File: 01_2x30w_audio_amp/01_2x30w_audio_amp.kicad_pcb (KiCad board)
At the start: 4 copper layers, 90 x 90 mm, 90 parts, among them J101 CUI 5.08mm, J102 SSQ-107-03-T-D, J103 SSQ-120-03-T-D, J104 CUI 5.08mm, J105 CUI 5.08mm, J108 CUI 5.08mm, J109 CUI 5.08mm, Q101 AON7534, Q201 AON7534, U101 MCP1416, U201 AP64500, U801 TPA3118D2

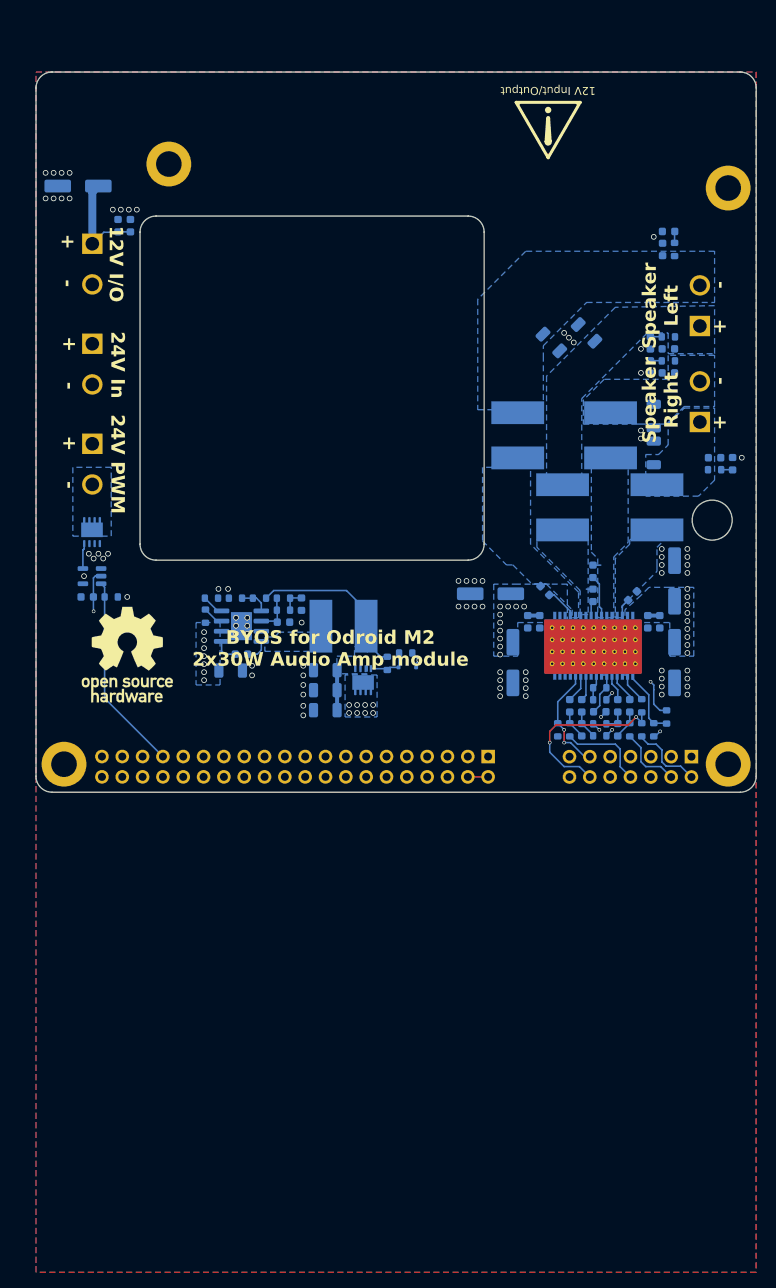
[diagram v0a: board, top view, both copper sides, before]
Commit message: Module no. 1 completely redesigned
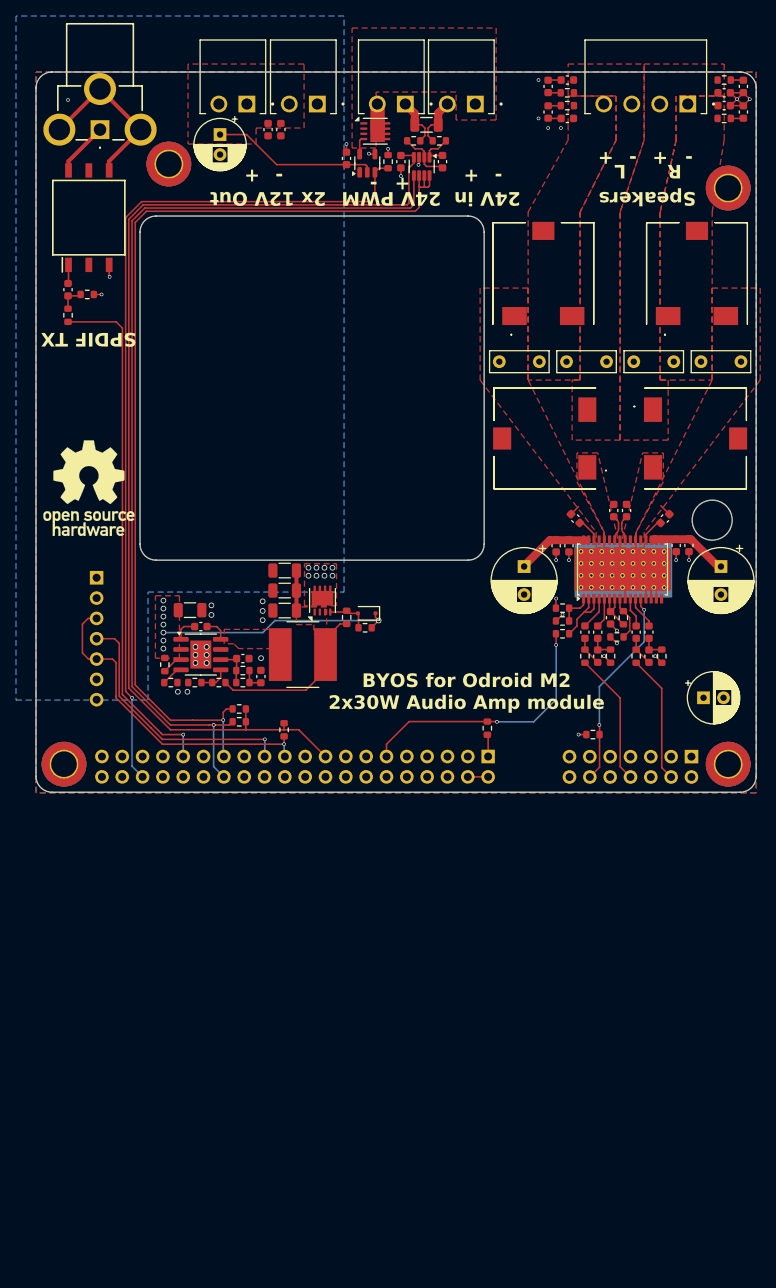
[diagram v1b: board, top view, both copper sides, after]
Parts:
- removed C817, C818, C819: 680n 35V, Capacitor_SMD:C_1206_3216Metric
- removed C820, C821, C826, C827: 865080545012, Capacitor_SMD:C_Elec_6.3x7.7
- removed the J101 at (27.0, 54.0)
- removed the J105 at (103.0, 51.7)
- removed J109: CUI 5.08mm, libs:CUI_TBP01R1-508-02BE
- removed L802, L803, L804: SRN8040TA-100M, Inductor_SMD:L_Bourns_SRN8040TA
- removed SYM102: SYM_Radioactive_Large, Symbol:Symbol_Attention_Triangle_8x7mm_Copper
- added C104: A750EK227M1CAAE016, Capacitor_THT:CP_Radial_D6.3mm_P2.50mm, F.Cu at (43.0, 27.8)
- added C301: 100n, Capacitor_SMD:C_0603_1608Metric, F.Cu at (24.0, 47.2)
- added C401: 100n 25V, Capacitor_SMD:C_0603_1608Metric, F.Cu at (65.6, 31.2)
- added C402: 100n, Capacitor_SMD:C_0603_1608Metric, F.Cu at (70.8, 31.2)
- added C616: B32529C684J, Capacitor_THT:C_Rect_L7.2mm_W2.5mm_P5.00mm_FKS2_FKP2_MKS2_MKP2, F.Cu at (77.9, 56.2)
- added C618: B32529C684J, Capacitor_THT:C_Rect_L7.2mm_W2.5mm_P5.00mm_FKS2_FKP2_MKS2_MKP2, F.Cu at (94.7, 56.2)
- added C619: B32529C684J, Capacitor_THT:C_Rect_L7.2mm_W2.5mm_P5.00mm_FKS2_FKP2_MKS2_MKP2, F.Cu at (108.1, 56.2)
- added C620: A750KS227M1EAAE015, Capacitor_THT:CP_Radial_D8.0mm_P3.50mm, F.Cu at (81.0, 81.8)
- added C621: A750KS227M1EAAE015, Capacitor_THT:CP_Radial_D8.0mm_P3.50mm, F.Cu at (105.6, 81.8)
- added J103: CUI 3.5mm, libs:CUI_TBP03R1-350-02BE, F.Cu at (74.9, 24.0)
- added J104: CUI 3.5mm, libs:CUI_TBP03R1-350-02BE, F.Cu at (66.2, 24.0)
- added J107: CUI 3.5mm, libs:CUI_TBP03R1-350-02BE, F.Cu at (46.4, 24.0)
- added J301: KLPX-0848A, libs:936, F.Cu at (28.0, 27.2)
- added J501: Conn_01x07, Connector_PinSocket_2.54mm:PinSocket_1x07_P2.54mm_Vertical, B.Cu at (27.6, 83.2)
- added L602: RFC0807B-123KE, libs:SER1360182KLD, F.Cu at (83.6, 65.8)
- added L603: RFC0807B-123KE, libs:SER1360182KLD, F.Cu at (102.4, 65.8)
- added L604: RFC0807B-123KE, libs:SER1360182KLD, F.Cu at (102.6, 45.2)
- added R301: 200R, Resistor_SMD:R_0603_1608Metric, F.Cu at (24.0, 50.4)
- added R302: 110R, Resistor_SMD:R_0603_1608Metric, F.Cu at (26.4, 47.8)
- added R401: 10k, Resistor_SMD:R_0603_1608Metric, F.Cu at (45.4, 99.6)
- added R402: 10k, Resistor_SMD:R_0603_1608Metric, F.Cu at (45.4, 101.2)
- added R403: 10R, Resistor_SMD:R_0603_1608Metric, F.Cu at (70.4, 28.6)
- added R404: 30m 1W, Resistor_SMD:R_1206_3216Metric, F.Cu at (68.8, 26.6)
- added R405: 10R, Resistor_SMD:R_0603_1608Metric, F.Cu at (67.2, 28.6)
- added R501: 10k, Resistor_SMD:R_0603_1608Metric, F.Cu at (51.0, 102.2)
- added T301: DA101JC, libs:SOP254P1270X635-6N, F.Cu at (26.6, 38.2)
- added U401: INA219AxDCN, Package_TO_SOT_SMD:SOT-23-8, F.Cu at (68.2, 31.8)
- C101, C103, C201, C202, C203, C204, D201, Q101, Q201, R201, R202, R203, R204, R205, R206, U101, U201: moved to F.Cu
- C102: renamed from C104; moved to F.Cu
- C105: value 865080545012 -> A750EK227M1CAAE016; footprint Capacitor_SMD:C_Elec_6.3x7.7 -> Capacitor_THT:CP_Radial_D6.3mm_P2.50mm; moved to F.Cu
- C210: renamed from C206; moved to F.Cu
- C212: renamed from C207; moved to F.Cu
- C215: renamed from C208; moved to F.Cu
- C601: renamed from C801; moved to F.Cu
- C602: renamed from C802; moved to F.Cu
- C603: renamed from C803; moved to F.Cu
- C604: renamed from C804; moved to F.Cu
- C605: renamed from C805; moved to F.Cu
- C606: renamed from C806; moved to F.Cu
- C607: renamed from C807; moved to F.Cu
- C608: renamed from C808; moved to F.Cu
- C609: renamed from C832; moved to F.Cu
- C610: renamed from C809; moved to F.Cu
- C611: renamed from C810; moved to F.Cu
- C612: renamed from C812; moved to F.Cu
- C613: renamed from C813; moved to F.Cu
- C614: renamed from C814; moved to F.Cu
- C615: renamed from C815; moved to F.Cu
- C617: renamed from C816; value 680n 35V -> B32529C684J; footprint Capacitor_SMD:C_1206_3216Metric -> Capacitor_THT:C_Rect_L7.2mm_W2.5mm_P5.00mm_FKS2_FKP2_MKS2_MKP2; moved to F.Cu
- C622: renamed from C823; moved to F.Cu
- C623: renamed from C822; moved to F.Cu
- C624: renamed from C824; moved to F.Cu
- C625: renamed from C825; moved to F.Cu
- C626: renamed from C829; moved to F.Cu
- C627: renamed from C828; moved to F.Cu
- C628: renamed from C830; moved to F.Cu
- C629: renamed from C831; moved to F.Cu
- H100: renamed from H101; footprint MountingHole:MountingHole_3.2mm_M3_DIN965_Pad -> MountingHole:MountingHole_3.2mm_M3_DIN965_Pad_TopBottom
- H101: renamed from H102; footprint MountingHole:MountingHole_3.2mm_M3_DIN965_Pad -> MountingHole:MountingHole_3.2mm_M3_DIN965_Pad_TopBottom
- H102: renamed from H103; footprint MountingHole:MountingHole_3.2mm_M3_DIN965_Pad -> MountingHole:MountingHole_3.2mm_M3_DIN965_Pad_TopBottom
- H103: renamed from H104; footprint MountingHole:MountingHole_3.2mm_M3_DIN965_Pad -> MountingHole:MountingHole_3.2mm_M3_DIN965_Pad_TopBottom
- J105: renamed from J104; value CUI 5.08mm -> CUI 3.5mm; footprint libs:CUI_TBP01R1-508-02BE -> libs:CUI_TBP03R1-350-04BE; moved to F.Cu
- J106: renamed from J108; value CUI 5.08mm -> CUI 3.5mm; footprint libs:CUI_TBP01R1-508-02BE -> libs:CUI_TBP03R1-350-02BE; moved to F.Cu
- L201: renamed from L202; moved to F.Cu
- L601: renamed from L801; value SRN8040TA-100M -> RFC0807B-123KE; footprint Inductor_SMD:L_Bourns_SRN8040TA -> libs:SER1360182KLD; moved to F.Cu
- R101: renamed from R105; moved to F.Cu
- R207: renamed from R208; moved to F.Cu
- R208: renamed from R207; moved to F.Cu
- R601: renamed from R801; moved to F.Cu
- R602: renamed from R802; moved to F.Cu
- R603: renamed from R803; moved to F.Cu
- R604: renamed from R804; moved to F.Cu
- R605: renamed from R805; moved to F.Cu
- R606: renamed from R806; moved to F.Cu
- R607: renamed from R807; moved to F.Cu
- R608: renamed from R808; moved to F.Cu
- R609: renamed from R809; moved to F.Cu
- R610: renamed from R810; moved to F.Cu
- R611: renamed from R811; moved to F.Cu
- R612: renamed from R813; moved to F.Cu
- R613: renamed from R812; moved to F.Cu
- R614: renamed from R814; moved to F.Cu
- R615: renamed from R815; moved to F.Cu
- U601: renamed from U801; moved to F.Cu
- moved C105 101.0 mm to (103.4, 98.2), turned to 0 degrees
- moved R101 64.5 mm to (64.0, 31.2), turned to -90 degrees
- moved C101 63.7 mm to (58.8, 30.8), turned to 90 degrees
- moved U101 62.0 mm to (61.4, 31.4), turned to 90 degrees
- moved Q101 61.3 mm to (62.4, 27.4), turned to 0 degrees
- moved C627 52.5 mm to (84.0, 21.8)
- moved C623 50.7 mm to (86.4, 21.0), turned to 0 degrees
- moved R613 50.6 mm to (86.4, 22.6), turned to 180 degrees
- moved J105 39.8 mm to (101.5, 24.0), turned to 180 degrees
- moved C626 34.3 mm to (84.0, 25.0)
- moved R612 34.3 mm to (86.4, 24.2)
- moved C622 34.2 mm to (86.4, 25.8)
- moved C628 34.1 mm to (108.4, 21.8)
- moved J106 33.1 mm to (55.2, 24.0), turned to 180 degrees
- moved R614 32.8 mm to (106.0, 21.0), turned to 0 degrees
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- renumbered J102 to J101, J103 to J102
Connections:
- net /GPIO1_B7 renamed /PWM13
- C608 pad 1: Net-(U801-BSNR) -> Net-(U601-BSPR)
- C608 pad 2: Net-(U801-OUTNR) -> Net-(U601-OUTPR)
- C609 pad 1: Net-(U801-BSPR) -> Net-(U601-BSNR)
- C609 pad 2: Net-(U801-OUTPR) -> Net-(U601-OUTNR)
- C617 pad 1: /Audio Power Amp/R+ -> /Audio Power Amp/R-
- C622 pad 2: /Audio Power Amp/R- -> /Audio Power Amp/R+
- C623 pad 2: /Audio Power Amp/R+ -> /Audio Power Amp/R-
- H100 pad 1: GND -> (no net)
- H101 pad 1: GND -> (no net)
- H102 pad 1: GND -> (no net)
- H103 pad 1: GND -> (no net)
- J102 pad 1: /+3V3_1 -> +3V3_1
- J102 pad 11: /UART9_RX -> /GPIO3_D4
- J102 pad 17: /+3V3_2 -> +3V3_2
- J102 pad 23: /UART9_~{CTS} -> /PWM10
- J102 pad 31: /GPIO1_B6 -> /SPDIF0_TX
- J102 pad 36: /GPIO4_B5 -> /PWM12
- J105 pad 1: /Audio Power Amp/R+ -> /Audio Power Amp/L-
- J105 pad 2: /Audio Power Amp/R- -> /Audio Power Amp/L+
- J106 pad 1: +12V -> GND
- J106 pad 2: GND -> +12V
- L601 pad 1: Net-(U801-OUTPR) -> Net-(U601-OUTPR)
- R101 pad 2: /PWM8 -> /PWM12
- R601 pad 1: +3V3 -> +3V3_1
- R601 pad 2: /GPIO3_C5 -> /GPIO3_D4
- R602 pad 2: /GPIO3_C4 -> /GPIO3_C5
- R603 pad 1: /HPR -> /HPL
- R605 pad 1: GND -> /HPR
- R606 pad 1: /HPL -> GND
- R611 pad 1: /GPIO3_C5 -> /GPIO3_D4
- R612 pad 1: /Audio Power Amp/R- -> /Audio Power Amp/R+
- R613 pad 1: /Audio Power Amp/R+ -> /Audio Power Amp/R-
- U101 pad 3: /PWM8 -> /PWM12
- U601 pad 12: /GPIO3_C4 -> /GPIO3_C5
- U601 pad 16: unconnected-(U801-SYNC-Pad16) -> /Audio Power Amp/SYNC
- U601 pad 26: Net-(U801-BSNR) -> Net-(U601-BSNR)
- U601 pad 27: Net-(U801-OUTNR) -> Net-(U601-OUTNR)
- U601 pad 29: Net-(U801-OUTPR) -> Net-(U601-OUTPR)
- U601 pad 30: Net-(U801-BSPR) -> Net-(U601-BSPR)
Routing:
- net +3V3_2: track 0.00 -> 133.9 mm
- net /I2C6_SDA: track 0.00 -> 122.1 mm, vias 0 -> 1
- net /I2C6_SCL: track 0.00 -> 119.6 mm, vias 0 -> 1
- net /PWM12: track 0.00 -> 107.9 mm, vias 0 -> 1
- net /SPDIF0_TX: track 0.00 -> 65.5 mm, vias 0 -> 1
- net +24V: track 10.2 -> 62.3 mm, vias 28 -> 9
- net /GPIO3_D1: track 0.00 -> 40.7 mm, vias 0 -> 1
- net /GPIO3_D4: track 0.00 -> 33.3 mm, vias 0 -> 2
- net /PWM10: track 0.00 -> 32.3 mm, vias 0 -> 1
- net GND: track 16.2 -> 42.2 mm, vias 82 -> 38
- net /PWM8: track 24.8 -> 0.00 mm
- net Net-(T301-SA): track 0.00 -> 21.1 mm
- net /GPIO3_C4: track 13.6 -> 0.65 mm, vias 2 -> 0
- net +3V3: track 9.29 -> 0.00 mm
- net /HPR: track 8.31 -> 16.1 mm
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- added copper zone on F.Cu, net +12V
- added copper zone on In2.Cu, net +12V
- added copper zone on F.Cu, net +24V
- added copper zone on In2.Cu, net +24V
- added copper zone on F.Cu, net /Audio Power Amp/L+
- added copper zone on F.Cu, net /Audio Power Amp/L-
- added copper zone on F.Cu, net /Audio Power Amp/R+
- added copper zone on F.Cu, net /Audio Power Amp/R-
- added copper zone on F.Cu, net Net-(C210-Pad1)
- added copper zone on F.Cu, net Net-(U201-SW)
- added copper zone on F.Cu, net Net-(U601-OUTNL)
- added copper zone on F.Cu, net Net-(U601-OUTNR)
- added copper zone on F.Cu, net Net-(U601-OUTPL)
- added copper zone on F.Cu, net Net-(U601-OUTPR)
- removed copper zone on In1.Cu, net +12V
- removed copper zone on B.Cu, net +24V
- removed copper zone on In1.Cu, net +24V
- removed copper zone on B.Cu, net /Audio Power Amp/L+
- removed copper zone on B.Cu, net /Audio Power Amp/L-
- removed copper zone on B.Cu, net /Audio Power Amp/R+
- removed copper zone on B.Cu, net /Audio Power Amp/R-
- removed copper zone on In2.Cu, net GND
- removed copper zone on B.Cu, net Net-(C210-Pad1)
- removed copper zone on B.Cu, net Net-(J104-Pin_2)
- removed copper zone on B.Cu, net Net-(U201-SW)
- removed copper zone on B.Cu, net Net-(U601-OUTNL)
- removed copper zone on B.Cu, net Net-(U601-OUTPL)
- removed copper zone on B.Cu, net Net-(U801-OUTNR)
- removed copper zone on B.Cu, net Net-(U801-OUTPR)
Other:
- board text added: "12V"
- board text added: "24V in"
- board text added: "2x 12V Out"
- board text added: "GND"
- board text added: "L"
- board text added: "PWM"
- board text added: "R"
- board text added: "SPDIF TX"
- board text added: "Speakers"
- board text added: "Tach"
- board text removed: "12V I/O"
- board text removed: "12V Input/Output"
- board text removed: "24V In"
- board text removed: "Speaker Left"
- board text removed: "Speaker Right"
